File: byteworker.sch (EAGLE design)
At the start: 55 parts, among them IC1 MCP1703, IC2 TJA1043, J2 AVRSPI-61.27, Q1 BSS138, Q2 BSS138, Q3 BSS138, Q5 BSS138, Q6 FDN5618P, X1 16 MHz, X2 bus connector

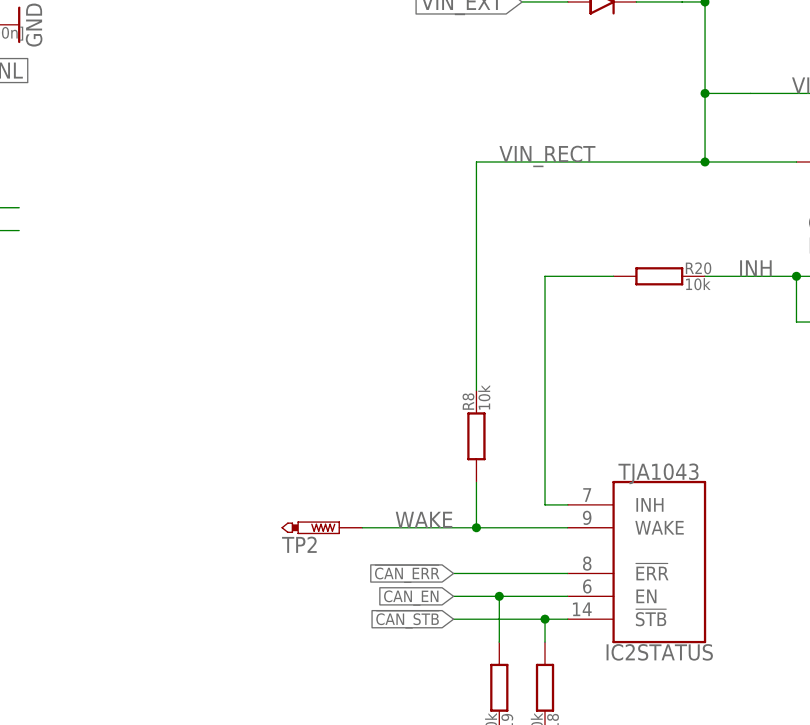
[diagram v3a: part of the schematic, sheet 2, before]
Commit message: - Shuffle some pins - Optional wake on input pins
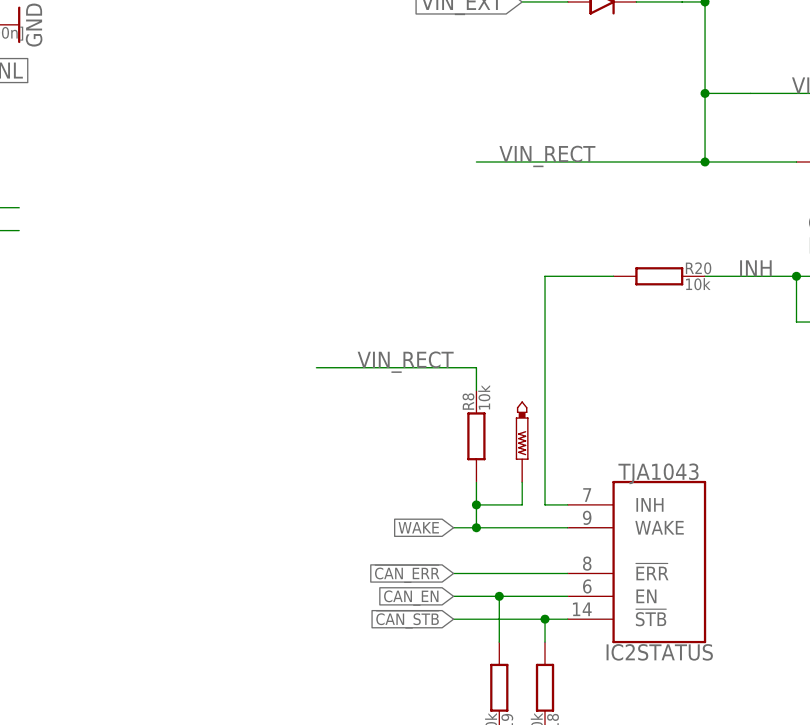
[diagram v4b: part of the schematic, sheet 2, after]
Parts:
- added C10: 100n, bytewerk-passive:C0603
- added JUMPER1: JUMPER-2_10, bytewerk-jumper:JUMPER-2_10
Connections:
- removed net TESTLED3: UC1PORTD.(PSCOUT0A)PD0
- new net PD0: JP3.6, UC1PORTD.(PSCOUT0A)PD0
- net +5V: now also C10.1, JP2.4; no longer JP3.4
- net CANH: now also JP3.8; no longer JP3.9
- net CANL: now also JP3.7; no longer JP3.8
- net D2A: now also JP3.4; no longer JP3.6
- net GND: now also C10.2, JP3.10
- net IN0: now also JUMPER1.2
- net PD1: now also JP3.5; no longer JP3.7
- net VIN_BUS: no longer JP3.5
- net WAKE: now also JP3.9, JUMPER1.1; no longer JP3.10
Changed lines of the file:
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@@
 <part name="LED2" library="bytewerk-led" deviceset="LED0603" device="" value="green"/>
 <part name="JP2" library="pinhead" deviceset="PINHD-1X8" device=""/>
+<part name="C10" library="bytewerk-passive" deviceset="C" device="0603" value="100n"/>
+<part name="JUMPER1" library="bytewerk-jumper" deviceset="JUMPER-2" device="_10"/>
 </parts>
 <sheets>
@@
 <text x="190.5" y="99.06" size="1.778" layer="98" rot="R180" align="center-right">7V to 16V</text>
 <text x="71.12" y="142.24" size="1.778" layer="98" align="center-left">max 50mA</text>
+<text x="147.32" y="73.66" size="1.778" layer="98" rot="R90" align="center-right">max 50mA</text>
 </plain>
 <instances>
@@
 <label x="134.62" y="142.24" size="1.27" layer="95" rot="MR0" xref="yes"/>
 </segment>
-<segment>
-<wire x1="175.26" y1="109.22" x2="167.64" y2="109.22" width="0.1524" layer="91"/>
-<label x="175.26" y="109.22" size="1.27" layer="95" xref="yes"/>
-<pinref part="JP3" gate="A" pin="5"/>
-</segment>
 </net>
 <net name="GND" class="0">
@@
 <label x="157.48" y="83.82" size="1.27" layer="95" rot="R270" xref="yes"/>
 </segment>
+<segment>
+<pinref part="JP3" gate="A" pin="10"/>
+<wire x1="167.64" y1="121.92" x2="175.26" y2="121.92" width="0.1524" layer="91"/>
+<label x="175.26" y="121.92" size="1.27" layer="95" xref="yes"/>
+</segment>
 </net>
 <net name="OUT1" class="0">
@@
 <net name="+5V" class="0">
 <segment>
-<wire x1="167.64" y1="106.68" x2="175.26" y2="106.68" width="0.1524" layer="91"/>
-<label x="175.26" y="106.68" size="1.27" layer="95" xref="yes"/>
-<pinref part="JP3" gate="A" pin="4"/>
-</segment>
-<segment>
 <pinref part="J2" gate="G$1" pin="+5V"/>
 <wire x1="55.88" y1="142.24" x2="60.96" y2="142.24" width="0.1524" layer="91"/>
 <label x="60.96" y="142.24" size="1.27" layer="95" xref="yes"/>
 </segment>
+<segment>
+<pinref part="JP2" gate="A" pin="4"/>
+<wire x1="147.32" y1="91.44" x2="147.32" y2="83.82" width="0.1524" layer="91"/>
+<label x="147.32" y="83.82" size="1.27" layer="95" rot="MR270" xref="yes"/>
+</segment>
 </net>
 <net name="CANH" class="0">
@@
 </segment>
 <segment>
-<wire x1="167.64" y1="119.38" x2="175.26" y2="119.38" width="0.1524" layer="91"/>
-<label x="175.26" y="119.38" size="1.27" layer="95" xref="yes"/>
-<pinref part="JP3" gate="A" pin="9"/>
+<label x="175.26" y="116.84" size="1.27" layer="95" xref="yes"/>
+<pinref part="JP3" gate="A" pin="8"/>
+<wire x1="175.26" y1="116.84" x2="167.64" y2="116.84" width="0.1524" layer="91"/>
 </segment>
 </net>
@@
 </segment>
 <segment>
-<wire x1="175.26" y1="116.84" x2="167.64" y2="116.84" width="0.1524" layer="91"/>
-<label x="175.26" y="116.84" size="1.27" layer="95" xref="yes"/>
-<pinref part="JP3" gate="A" pin="8"/>
+<label x="175.26" y="114.3" size="1.27" layer="95" xref="yes"/>
+<pinref part="JP3" gate="A" pin="7"/>
+<wire x1="175.26" y1="114.3" x2="167.64" y2="114.3" width="0.1524" layer="91"/>
 </segment>
 </net>
@@
 <net name="D2A" class="0">
 <segment>
-<wire x1="167.64" y1="111.76" x2="175.26" y2="111.76" width="0.1524" layer="91"/>
-<label x="175.26" y="111.76" size="1.27" layer="95" xref="yes"/>
-<pinref part="JP3" gate="A" pin="6"/>
+<label x="175.26" y="106.68" size="1.27" layer="95" xref="yes"/>
+<pinref part="JP3" gate="A" pin="4"/>
+<wire x1="175.26" y1="106.68" x2="167.64" y2="106.68" width="0.1524" layer="91"/>
 </segment>
 </net>
 <net name="WAKE" class="0">
 <segment>
-<wire x1="167.64" y1="121.92" x2="175.26" y2="121.92" width="0.1524" layer="91"/>
-<label x="175.26" y="121.92" size="1.27" layer="95" xref="yes"/>
-<pinref part="JP3" gate="A" pin="10"/>
+<label x="175.26" y="119.38" size="1.27" layer="95" xref="yes"/>
+<pinref part="JP3" gate="A" pin="9"/>
+<wire x1="175.26" y1="119.38" x2="167.64" y2="119.38" width="0.1524" layer="91"/>
 </segment>
 </net>
@@
 <net name="PD1" class="0">
 <segment>
-<wire x1="167.64" y1="114.3" x2="175.26" y2="114.3" width="0.1524" layer="91"/>
-<label x="175.26" y="114.3" size="1.27" layer="95" xref="yes"/>
-<pinref part="JP3" gate="A" pin="7"/>
+<label x="175.26" y="109.22" size="1.27" layer="95" xref="yes"/>
+<pinref part="JP3" gate="A" pin="5"/>
+<wire x1="175.26" y1="109.22" x2="167.64" y2="109.22" width="0.1524" layer="91"/>
 </segment>
 </net>
@@
 <label x="175.26" y="104.14" size="1.27" layer="95" xref="yes"/>
 <pinref part="JP3" gate="A" pin="3"/>
+</segment>
+</net>
+<net name="PD0" class="0">
+<segment>
+<pinref part="JP3" gate="A" pin="6"/>
+<wire x1="167.64" y1="111.76" x2="175.26" y2="111.76" width="0.1524" layer="91"/>
+<label x="175.26" y="111.76" size="1.27" layer="95" xref="yes"/>
 </segment>
 </net>
@@
 <instance part="GND11" gate="1" x="58.42" y="106.68" rot="MR0"/>
 <instance part="D4" gate="G$1" x="205.74" y="147.32" rot="R180"/>
-<instance part="TP2" gate="G$1" x="116.84" y="91.44" rot="MR90"/>
+<instance part="TP2" gate="G$1" x="137.16" y="99.06" smashed="yes" rot="MR180">
+<attribute name="TP_SIGNAL_NAME" x="138.43" y="101.6" size="1.778" layer="97" rot="MR180"/>
+</instance>
 <instance part="R8" gate="G$1" x="132.08" y="101.6" rot="R90"/>
 <instance part="C8" gate="G$1" x="63.5" y="114.3" rot="MR270"/>
@@
 <pinref part="D5" gate="G$1" pin="C"/>
 <wire x1="149.86" y1="154.94" x2="157.48" y2="154.94" width="0.1524" layer="91"/>
-<pinref part="R8" gate="G$1" pin="2"/>
-<wire x1="132.08" y1="106.68" x2="132.08" y2="132.08" width="0.1524" layer="91"/>
 <wire x1="132.08" y1="132.08" x2="157.48" y2="132.08" width="0.1524" layer="91"/>
 <label x="134.62" y="132.08" size="1.778" layer="95"/>
@@
 <wire x1="50.8" y1="127" x2="81.28" y2="127" width="0.1524" layer="91"/>
 <label x="53.34" y="127" size="1.778" layer="95"/>
+</segment>
+<segment>
+<pinref part="R8" gate="G$1" pin="2"/>
+<wire x1="132.08" y1="106.68" x2="132.08" y2="109.22" width="0.1524" layer="91"/>
+<wire x1="132.08" y1="109.22" x2="114.3" y2="109.22" width="0.1524" layer="91"/>
+<label x="129.54" y="109.22" size="1.778" layer="95" rot="MR0"/>
 </segment>
 </net>
@@
 <segment>
 <pinref part="IC2" gate="STATUS" pin="WAKE"/>
-<label x="129.54" y="91.44" size="1.778" layer="95" rot="MR0"/>
+<label x="129.54" y="91.44" size="1.27" layer="95" rot="MR0" xref="yes"/>
 <pinref part="R8" gate="G$1" pin="1"/>
-<wire x1="132.08" y1="96.52" x2="132.08" y2="91.44" width="0.1524" layer="91"/>
+<wire x1="132.08" y1="96.52" x2="132.08" y2="93.98" width="0.1524" layer="91"/>
 <junction x="132.08" y="91.44"/>
 <pinref part="TP2" gate="G$1" pin="TP"/>
-<wire x1="132.08" y1="91.44" x2="119.38" y2="91.44" width="0.1524" layer="91"/>
+<wire x1="132.08" y1="93.98" x2="132.08" y2="91.44" width="0.1524" layer="91"/>
 <wire x1="132.08" y1="91.44" x2="142.24" y2="91.44" width="0.1524" layer="91"/>
+<wire x1="132.08" y1="91.44" x2="129.54" y2="91.44" width="0.1524" layer="91"/>
+<junction x="132.08" y="93.98"/>
+<wire x1="137.16" y1="96.52" x2="137.16" y2="93.98" width="0.1524" layer="91"/>
+<wire x1="137.16" y1="93.98" x2="132.08" y2="93.98" width="0.1524" layer="91"/>
 </segment>
 </net>
@@
 <instance part="U$1" gate="G$1" x="121.92" y="43.18"/>
 <instance part="LED2" gate="G$1" x="114.3" y="48.26"/>
+<instance part="C10" gate="G$1" x="180.34" y="81.28" rot="R180"/>
+<instance part="JUMPER1" gate="G$1" x="180.34" y="149.86"/>
 </instances>
 <busses>
@@
 <wire x1="175.26" y1="76.2" x2="175.26" y2="71.12" width="0.1524" layer="91"/>
 <junction x="175.26" y="71.12"/>
+<pinref part="C10" gate="G$1" pin="2"/>
+<wire x1="177.8" y1="81.28" x2="175.26" y2="81.28" width="0.1524" layer="91"/>
+<wire x1="175.26" y1="81.28" x2="175.26" y2="76.2" width="0.1524" layer="91"/>
+<junction x="175.26" y="76.2"/>
 </segment>
 <segment>
@@
 <net name="+5V" class="0">
 <segment>
-<pinref part="C6" gate="G$1" pin="1"/>
-<pinref part="UC1" gate="SPECIAL" pin="AVCC"/>
-<wire x1="185.42" y1="76.2" x2="187.96" y2="76.2" width="0.1524" layer="91"/>
 <pinref part="UC1" gate="SPECIAL" pin="VCC"/>
-<wire x1="187.96" y1="76.2" x2="190.5" y2="76.2" width="0.1524" layer="91"/>
 <wire x1="190.5" y1="81.28" x2="187.96" y2="81.28" width="0.1524" layer="91"/>
 <wire x1="187.96" y1="81.28" x2="187.96" y2="86.36" width="0.1524" layer="91"/>
-<wire x1="187.96" y1="76.2" x2="187.96" y2="81.28" width="0.1524" layer="91"/>
-<junction x="187.96" y="76.2"/>
 <junction x="187.96" y="81.28"/>
 <pinref part="P+5" gate="1" pin="+5V"/>
+<pinref part="C10" gate="G$1" pin="1"/>
+<wire x1="187.96" y1="81.28" x2="185.42" y2="81.28" width="0.1524" layer="91"/>
+<pinref part="UC1" gate="SPECIAL" pin="AVCC"/>
+<wire x1="187.96" y1="76.2" x2="190.5" y2="76.2" width="0.1524" layer="91"/>
+<pinref part="C6" gate="G$1" pin="1"/>
+<wire x1="185.42" y1="76.2" x2="187.96" y2="76.2" width="0.1524" layer="91"/>
+<wire x1="187.96" y1="81.28" x2="187.96" y2="76.2" width="0.1524" layer="91"/>
+<junction x="187.96" y="76.2"/>
 </segment>
 <segment>
@@
 <segment>
 <pinref part="R12" gate="G$1" pin="2"/>
-<wire x1="172.72" y1="147.32" x2="172.72" y2="160.02" width="0.1524" layer="91"/>
-<label x="172.72" y="149.86" size="1.778" layer="95" rot="MR90"/>
+<wire x1="172.72" y1="147.32" x2="172.72" y2="149.86" width="0.1524" layer="91"/>
+<label x="172.72" y="154.94" size="1.778" layer="95" rot="MR90"/>
+<pinref part="JUMPER1" gate="G$1" pin="2"/>
+<wire x1="172.72" y1="149.86" x2="172.72" y2="162.56" width="0.1524" layer="91"/>
+<wire x1="177.8" y1="149.86" x2="172.72" y2="149.86" width="0.1524" layer="91"/>
+<junction x="172.72" y="149.86"/>
 </segment>
 </net>
@@
 </segment>
 </net>
-<net name="TESTLED3" class="0">
+<net name="PD0" class="0">
 <segment>
 <pinref part="UC1" gate="PORTD" pin="(PSCOUT0A)PD0"/>
@@
 </segment>
 </net>
+<net name="WAKE" class="0">
+<segment>
+<pinref part="JUMPER1" gate="G$1" pin="1"/>
+<wire x1="182.88" y1="149.86" x2="187.96" y2="149.86" width="0.1524" layer="91"/>
+<label x="187.96" y="149.86" size="1.778" layer="95" xref="yes"/>
+</segment>
+</net>

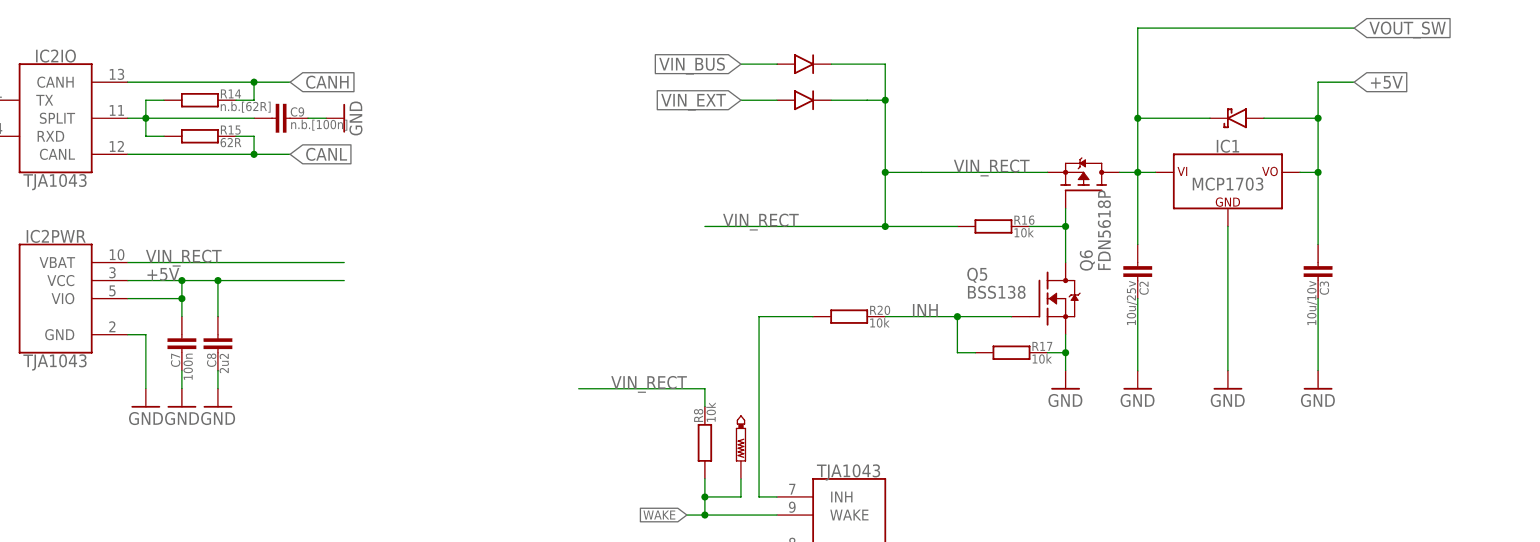
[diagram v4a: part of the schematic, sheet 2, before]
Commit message: - Some fixes in the schematics suggested by struppi - an incomplete board layout
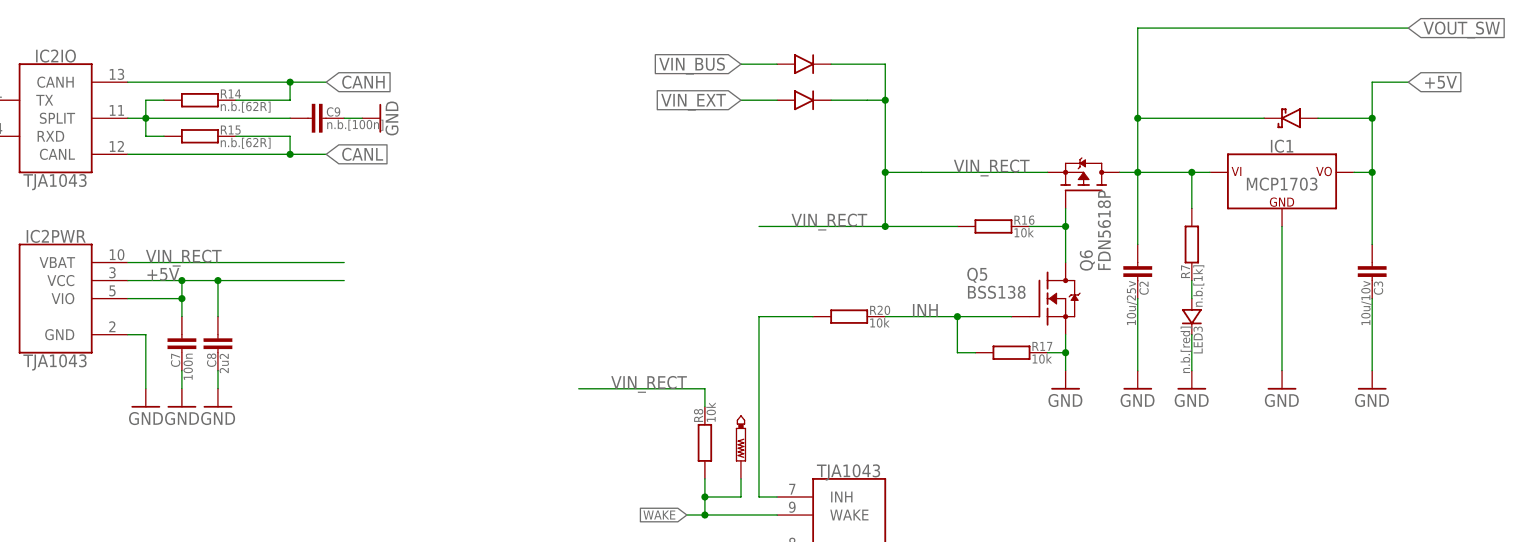
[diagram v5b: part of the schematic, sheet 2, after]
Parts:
- removed D4: SMS7630, bytewerk-passive:SMS7630
- removed JUMPER1: JUMPER-2_10, bytewerk-jumper:JUMPER-2_10
- added D6: SCHOTTKY323, bytewerk-passive:SCHOTTKY323
- added LED3: n.b.[red], bytewerk-led:LED0603
- added R7: n.b.[1k], bytewerk-passive:R0603
- LED1: value red -> n.b.[yellow]
- LED2: value green -> n.b.[green]
- R15: value 62R -> n.b.[62R]
- R21, R22: value 1k -> n.b.[1k]
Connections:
- new net N$8: LED3.A, R7.2
- net +5V: now also D6.A, JP2.3; no longer D4.A, JP2.4
- net CANH: now also JP3.7; no longer JP3.8
- net CANL: now also JP3.8; no longer JP3.7
- net GND: now also LED3.C
- net IN0: no longer JUMPER1.2
- net VOUT_SW: now also D6.C, R7.1; no longer D4.C
- net WAKE: no longer JUMPER1.1
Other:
- moved on the sheet: C3, C9, IC1

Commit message: v0.2: - Changed resistor values - Re-aligned pinheaders
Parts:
- R10, R2, R5: value 10k -> 1k
- R21, R22: value n.b.[1k] -> 1k
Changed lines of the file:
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@@
 <part name="R1" library="bytewerk-rcl" deviceset="R" device="0603" value="10k"/>
 <part name="GND4" library="supply1" deviceset="GND" device=""/>
-<part name="R2" library="bytewerk-rcl" deviceset="R" device="0603" value="10k"/>
+<part name="R2" library="bytewerk-rcl" deviceset="R" device="0603" value="1k"/>
 <part name="R3" library="bytewerk-rcl" deviceset="R" device="0603" value="dnp"/>
 <part name="P+1" library="supply1" deviceset="+5V" device=""/>
@@
 <part name="R4" library="bytewerk-rcl" deviceset="R" device="0603" value="10k"/>
 <part name="GND5" library="supply1" deviceset="GND" device=""/>
-<part name="R5" library="bytewerk-rcl" deviceset="R" device="0603" value="10k"/>
+<part name="R5" library="bytewerk-rcl" deviceset="R" device="0603" value="1k"/>
 <part name="R6" library="bytewerk-rcl" deviceset="R" device="0603" value="dnp"/>
 <part name="P+2" library="supply1" deviceset="+5V" device=""/>
@@
 <part name="R9" library="bytewerk-rcl" deviceset="R" device="0603" value="10k"/>
 <part name="GND19" library="supply1" deviceset="GND" device=""/>
-<part name="R10" library="bytewerk-rcl" deviceset="R" device="0603" value="10k"/>
+<part name="R10" library="bytewerk-rcl" deviceset="R" device="0603" value="1k"/>
 <part name="R11" library="bytewerk-rcl" deviceset="R" device="0603" value="dnp"/>
 <part name="P+3" library="supply1" deviceset="+5V" device=""/>
-<part name="R21" library="bytewerk-passive" deviceset="R" device="0603" value="n.b.[1k]"/>
-<part name="R22" library="bytewerk-passive" deviceset="R" device="0603" value="n.b.[1k]"/>
+<part name="R21" library="bytewerk-passive" deviceset="R" device="0603" value="1k"/>
+<part name="R22" library="bytewerk-passive" deviceset="R" device="0603" value="1k"/>
 <part name="J2" library="bytewerk-con" deviceset="AVRSPI-6" device="1.27"/>
 <part name="JP1" library="pinhead" deviceset="PINHD-1X10" device=""/>

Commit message: Done routing
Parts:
- removed Q6: FDN5618P, bytewerk-fet:FDN5618P
- removed X2: bus connector, con-subd:F09D
- added D4: 16V, bytewerk-diode:ZENER_PTVS18VP1UP
- added Q4: AP2321GN-HF-3TR, bytewerk-transistor:AP2321GN-HF-3TR
- added X3: SUBD-H9, bytewerk-con:SUBD-H9
- C2: value 10u/25v -> 1u/25V
- C3: value 10u/10v -> 1u/10V
- JP2: device pinhead:PINHD-1X8 -> pinhead:PINHD-1X6
- LED1: value n.b.[yellow] -> green
- LED2: value n.b.[green] -> blue
- LED3: value n.b.[red] -> red
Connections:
- net +5V: now also JP3.10; no longer JP2.3
- net CANH: now also X37.F; no longer X2.7
- net CANL: now also X32.F; no longer X2.2
- net GND: now also D4.A, JP2.6, X33.F; no longer JP2.8, JP3.10, X2.5
- net N$6: now also Q4.G; no longer Q6.G
- net OUT0: now also JP2.5; no longer JP2.7
- net OUT1: now also JP2.4; no longer JP2.6
- net OUT2: now also JP2.3; no longer JP2.5
- net VIN_BUS: now also X39.F; no longer X2.1
- net VIN_RECT: now also D4.C, Q4.S; no longer Q6.S
- net VOUT_SW: now also Q4.D; no longer Q6.D
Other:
- moved on the sheet: LED1, LED2, R21, R22
